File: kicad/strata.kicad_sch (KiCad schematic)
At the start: 100 parts, among them J1 Eurorack Mono Jack, J10 Conn_01x02_Male, J11 Conn_01x04_Male, J12 Conn_01x04_Female, J13 Conn_01x08_Male, J14 Eurorack Mono Jack, J15 Conn_01x08_Female, J16 Eurorack Mono Jack, J17 Eurorack Mono Jack, J18 Eurorack Mono Jack, J19 Eurorack Mono Jack, J2 Eurorack Mono Jack, J20 Eurorack Mono Jack, J24 Eurorack Mono Jack, J25 Eurorack Mono Jack, J26 Eurorack Mono Jack, J27 Eurorack Mono Jack, J28 Eurorack Mono Jack, J29 Eurorack Mono Jack, J3 Eurorack Mono Jack, J30 Eurorack Mono Jack, J31 Eurorack Mono Jack, J32 Conn_01x06_Female, J33 Eurorack Mono Jack, J34 Conn_01x06_Male, J35 Conn_01x08_Female, J36 Conn_01x08_Male, J37 Eurorack Power Small, J38 Conn_02x04_Odd_Even, J39 Conn_01x03_Male, J4 Eurorack Mono Jack, J49 Eurorack Mono Jack, J5 Conn_01x04_Female, J50 Eurorack Mono Jack, J51 Eurorack Mono Jack, J52 Conn_01x04_Female, J53 Conn_01x04_Male, J6 Conn_01x06_Female, J7 Conn_01x04_Male, J8 Conn_01x06_Male, J9 Conn_01x02_Female, Q17 2N3904, U1 TL072, U2 L78L05_TO92

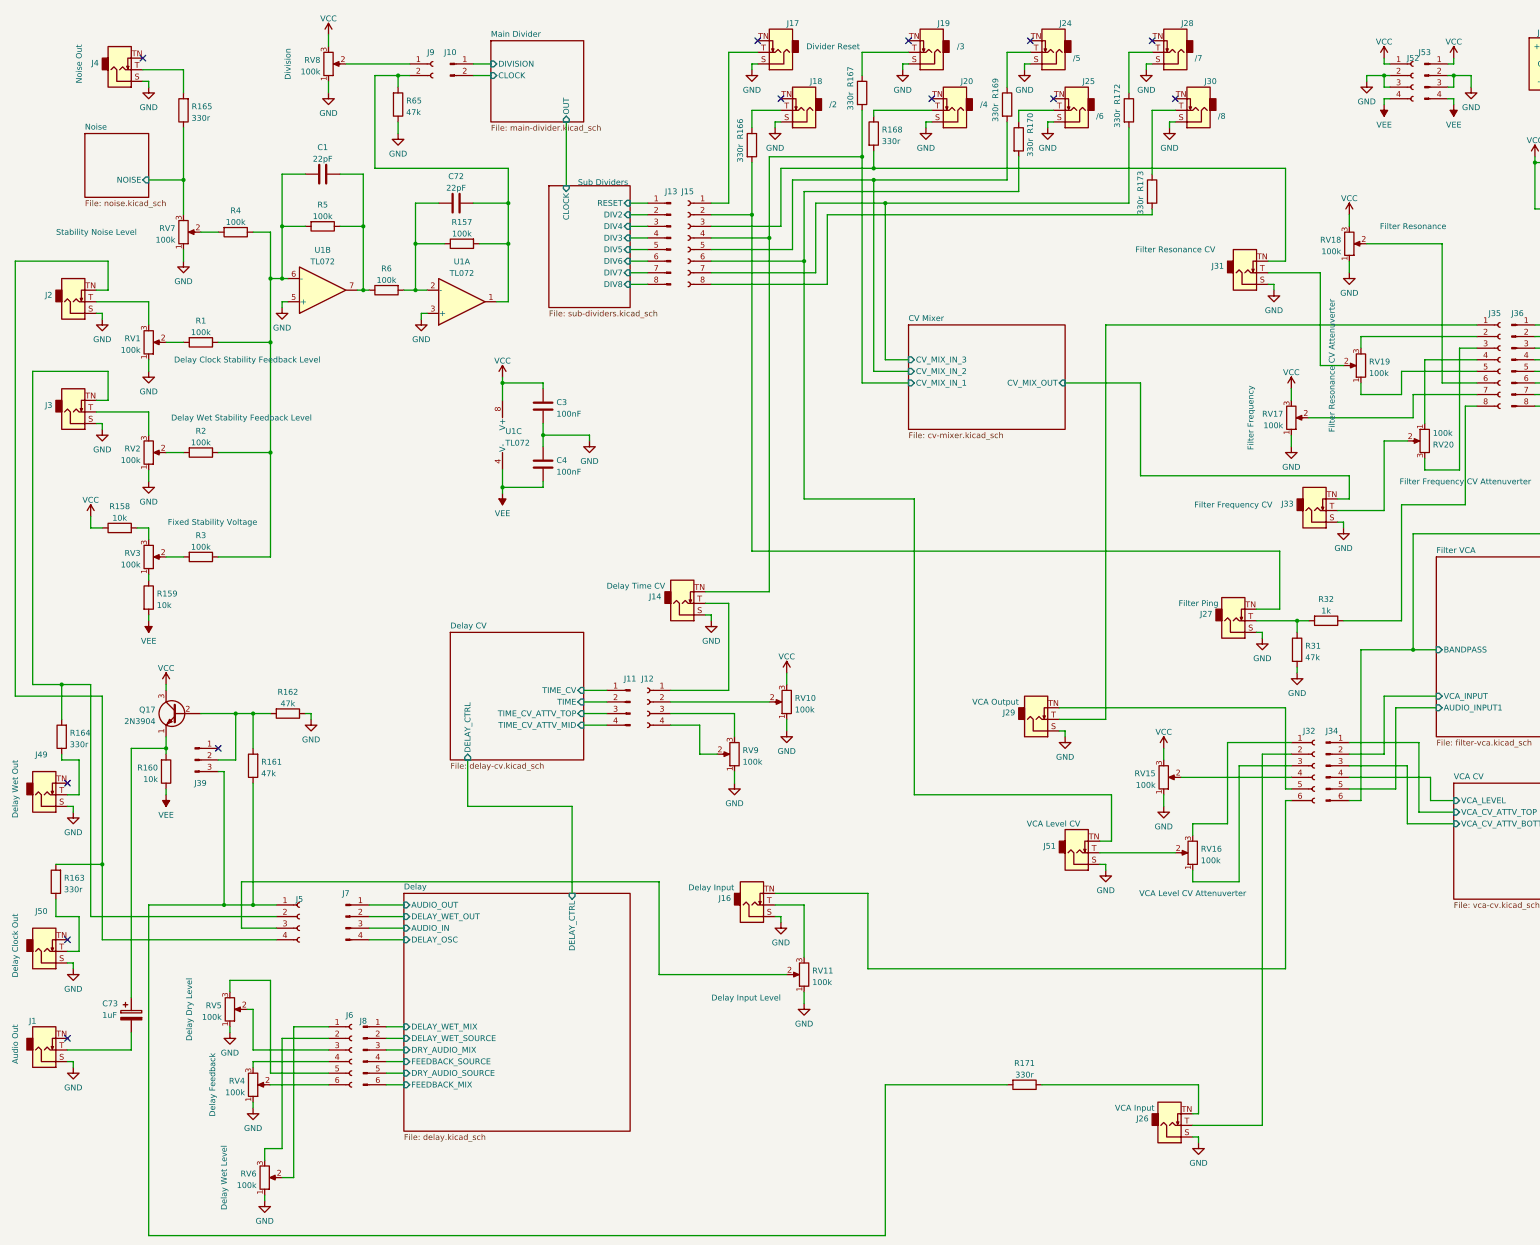
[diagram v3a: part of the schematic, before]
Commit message: Full rejig to use attiny for divider
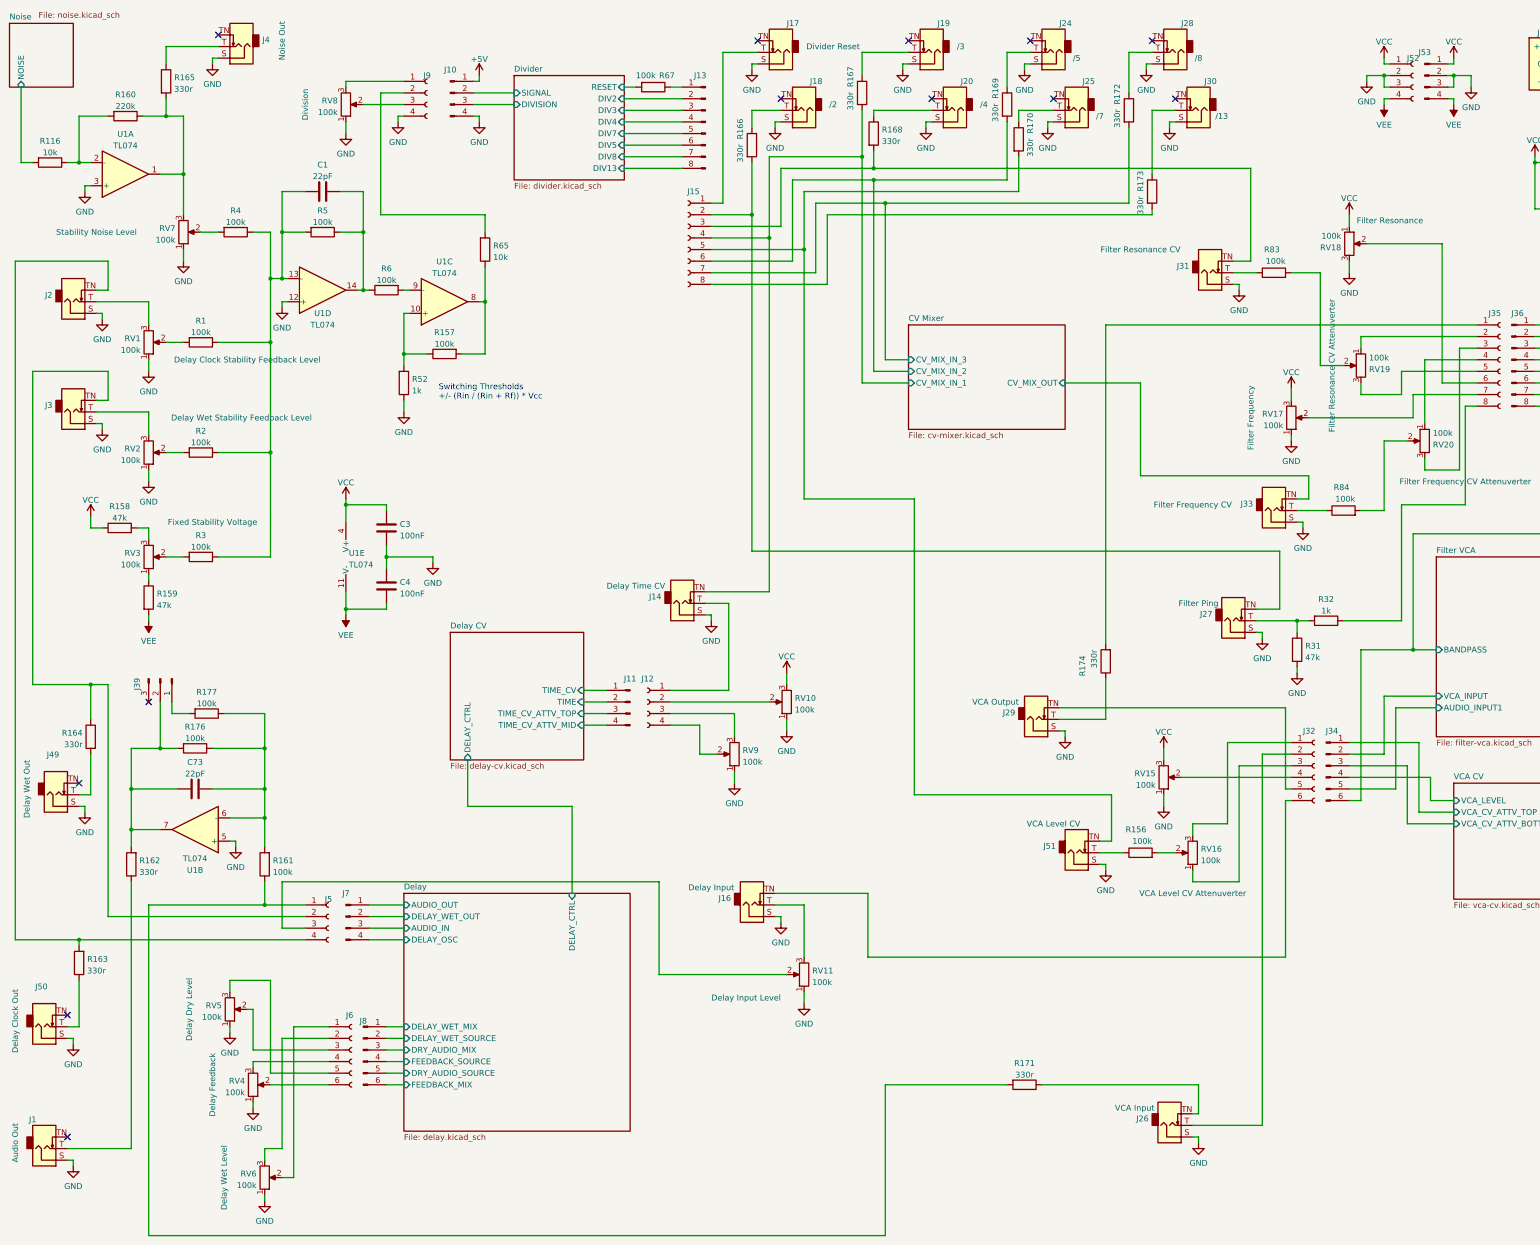
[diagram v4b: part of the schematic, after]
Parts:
- removed C72: 22pF, rumblesan-standard-parts:C_Rect_L7.0mm_W2.5mm_P5.00mm, symbol rumblesan-standard-parts:C
- removed C73: 1uF, rumblesan-standard-parts:CP_Radial_D5.0mm_P2.00mm, symbol rumblesan-standard-parts:C_Polarized
- removed J10: Conn_01x02_Male, Connector_PinHeader_2.54mm:PinHeader_1x02_P2.54mm_Vertical, symbol Connector:Conn_01x02_Male
- removed J9: Conn_01x02_Female, Connector_PinSocket_2.54mm:PinSocket_1x02_P2.54mm_Vertical, symbol Connector:Conn_01x02_Female
- removed Q17: 2N3904, Package_TO_SOT_THT:TO-92_Inline_Wide, symbol Transistor_BJT:2N3904
- removed U1: TL072, rumblesan-standard-parts:DIP-8_W7.62mm_Socket, symbol Amplifier_Operational:TL072
- added C73: 22pF, rumblesan-standard-parts:C_Rect_L7.0mm_W2.5mm_P5.00mm, symbol rumblesan-standard-parts:C
- added J10: Conn_01x04_Male, Connector_PinHeader_2.54mm:PinHeader_1x04_P2.54mm_Vertical, symbol Connector:Conn_01x04_Male
- added J9: Conn_01x04_Female, Connector_PinSocket_2.54mm:PinSocket_1x04_P2.54mm_Vertical, symbol Connector:Conn_01x04_Female
- added R116: 10k, rumblesan-standard-parts:R_Axial_DIN0207_L6.3mm_D2.5mm_P10.16mm_Horizontal, symbol rumblesan-standard-parts:R
- added R156, R176, R177, R67, R83, R84: 100k, rumblesan-standard-parts:R_Axial_DIN0207_L6.3mm_D2.5mm_P10.16mm_Horizontal, symbol rumblesan-standard-parts:R
- added R174: 330r, rumblesan-standard-parts:R_Axial_DIN0207_L6.3mm_D2.5mm_P10.16mm_Horizontal, symbol rumblesan-standard-parts:R
- added R52: 1k, rumblesan-standard-parts:R_Axial_DIN0207_L6.3mm_D2.5mm_P10.16mm_Horizontal, symbol rumblesan-standard-parts:R
- added U1: TL074, rumblesan-standard-parts:DIP-14_W7.62mm_Socket, symbol Amplifier_Operational:TL074
- C3, C4: Spec ceramic C0G -> ceramic X7R
- J25: Name /6 -> /7
- J28: Name /7 -> /8
- J30: Name /8 -> /13
- R158, R159: value 10k -> 47k
- R160: value 10k -> 220k
- R161: value 47k -> 100k
- R162: value 47k -> 330r; footprint rumblesan-standard-parts:R_Axial_DIN0207_L6.3mm_D2.5mm_P2.54mm_Vertical -> rumblesan-standard-parts:R_Axial_DIN0207_L6.3mm_D2.5mm_P10.16mm_Horizontal
- R164: footprint rumblesan-standard-parts:R_Axial_DIN0207_L6.3mm_D2.5mm_P2.54mm_Vertical -> rumblesan-standard-parts:R_Axial_DIN0207_L6.3mm_D2.5mm_P10.16mm_Horizontal
- R65: value 47k -> 10k
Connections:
- net +5V: now also J10.1 (Pin_1)
- net CV Mixer/CV_MIX_IN_2: now also J15.6 (Pin_6); no longer J15.5 (Pin_5)
- net GND: now also RV18.3, J10.4 (Pin_4), J9.4 (Pin_4), R52.1, U1.12 (+), U1.3 (+), U1.5 (+); no longer R162.1, R65.1, RV18.1
- net Noise/NOISE: now also R116.2; no longer R165.1, RV7.3
- net VCC: now also RV18.1, U1.4 (V+); no longer RV18.3, RV8.3
- net VEE: now also U1.11 (V-); no longer R160.1
- net at R157.2: now also R65.1, U1.8; no longer R65.2
- net at R157.1: now also R52.2, U1.10 (+); no longer R6.2
- net at R165.2: now also R160.1, RV7.3, U1.1; no longer J4.T (Tip)
- net at J5.1 (Pin_1), R161.1, R171.2: no longer J39.3 (Pin_3)
- net at C1.1, R1.1, R2.1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: now also U1.13 (-)
- net at J3.TN (Tip_normalize), J5.2 (Pin_2): now also R164.1; no longer R164.2
- net at J49.T (Tip): now also R164.2; no longer R164.1
- net at C1.2, R5.1, R6.1: now also U1.14
- net at J35.1 (Pin_1): now also R174.2; no longer J29.T (Tip)
- net at J35.2 (Pin_2): now also RV19.1; no longer RV19.3
- net at J35.5 (Pin_5): now also RV19.3; no longer RV19.1
- net at R160.2: now also R116.1, U1.2 (-)
- net at J39.2 (Pin_2), R162.2: now also C73.2, R176.2, U1.7; no longer R161.2
- net at J31.T (Tip): now also R83.1; no longer RV19.2
- net at J33.T (Tip): now also R84.1; no longer RV20.2
- net at J51.TN (Tip_normalize), R170.2: now also J15.5 (Pin_5); no longer J15.6 (Pin_6)
- net at J51.T (Tip): now also R156.1; no longer RV16.2
- net at RV8.2: now also J9.3 (Pin_3)
- net at J1.T (Tip): now also R162.1
- net at J39.1 (Pin_1): now also R177.2
- net Sub Dividers/DIV2 renamed Divider/DIV2
- net Sub Dividers/DIV3 renamed Divider/DIV4
- net Sub Dividers/DIV4 renamed Divider/DIV3
- net Sub Dividers/DIV5 renamed Divider/DIV7
- net Sub Dividers/DIV6 renamed Divider/DIV5
- net Sub Dividers/DIV7 renamed Divider/DIV8
- net Sub Dividers/DIV8 renamed Divider/DIV13
- net Sub Dividers/RESET: no longer names the net of J13.1 (Pin_1)
- net Sub Dividers/RESET: now also R67.1
- new net: J4.T (Tip), R165.1
- new net: R84.2, RV20.2
- new net: J9.2 (Pin_2), R65.2
- new net: C73.1, R161.2, R176.1, R177.1, U1.6 (-)
- new net: R156.2, RV16.2
- new net: R83.2, RV19.2
- new net: R6.2, U1.9 (-)
- new net: J9.1 (Pin_1), RV8.3
- new net: J29.T (Tip), R174.1
- new net Divider/DIVISION: J10.3 (Pin_3)
- new net Divider/RESET: R67.2
- new net Divider/SIGNAL: J10.2 (Pin_2)
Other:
- removed sheet Main Divider
- removed sheet Sub Dividers
- added sheet Divider (divider.kicad_sch)
- note added: "Switching Thresholds +/- (Rin / (Rin + Rf)) * Vcc"
- moved on the sheet: C1, C3, C4, J1, J13, J31, J33, J4, J49, J5, J50, R157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

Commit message: Finished most recent redesign
probably still needs fixing though
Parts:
- C6: footprint rumblesan-standard-parts:CP_Radial_D5.0mm_P2.00mm -> rumblesan-standard-parts:CP_Radial_D5.0mm_L11.0mm_P2.00mm_Horizontal
- C7: footprint rumblesan-standard-parts:CP_Radial_D5.0mm_P2.00mm -> rumblesan-standard-parts:CP_Radial_D6.3.0mm_L11.0mm_P2.00mm_Horizontal
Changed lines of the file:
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@@
       (effects (font (size 1.27 1.27)) (justify left))
     )
-    (property "Footprint" "rumblesan-standard-parts:CP_Radial_D5.0mm_P2.00mm" (id 2) (at 401.32 51.1048 0)
+    (property "Footprint" "rumblesan-standard-parts:CP_Radial_D6.3.0mm_L11.0mm_P2.00mm_Horizontal" (id 2) (at 401.32 51.1048 0)
       (effects (font (size 1.27 1.27)) hide)
     )
@@
       (effects (font (size 1.27 1.27)) (justify left))
     )
-    (property "Footprint" "rumblesan-standard-parts:CP_Radial_D5.0mm_P2.00mm" (id 2) (at 401.32 38.4048 0)
+    (property "Footprint" "rumblesan-standard-parts:CP_Radial_D5.0mm_L11.0mm_P2.00mm_Horizontal" (id 2) (at 401.32 38.4048 0)
       (effects (font (size 1.27 1.27)) hide)
     )
@@
     )
     (path "/d1c4b4fd-5762-4000-9df8-83bd7b665ce2"
-      (reference "C6") (unit 1) (value "10uF") (footprint "rumblesan-standard-parts:CP_Radial_D5.0mm_P2.00mm")
+      (reference "C6") (unit 1) (value "10uF") (footprint "rumblesan-standard-parts:CP_Radial_D5.0mm_L11.0mm_P2.00mm_Horizontal")
     )
     (path "/5bf0b729-aac6-4585-bac0-2e1a7ffbf3b9"
-      (reference "C7") (unit 1) (value "10uF") (footprint "rumblesan-standard-parts:CP_Radial_D5.0mm_P2.00mm")
+      (reference "C7") (unit 1) (value "10uF") (footprint "rumblesan-standard-parts:CP_Radial_D6.3.0mm_L11.0mm_P2.00mm_Horizontal")
     )
     (path "/256127d0-0479-4408-a803-d00b3565e635/8fedaf81-144e-4069-b4a7-05f99da9d028"
@@
     )
     (path "/256127d0-0479-4408-a803-d00b3565e635/1b5de37d-f3ae-40d3-a60b-d8d12b5426c7"
-      (reference "C13") (unit 1) (value "10uF") (footprint "rumblesan-standard-parts:CP_Radial_D5.0mm_P2.00mm")
+      (reference "C13") (unit 1) (value "10uF") (footprint "rumblesan-standard-parts:CP_Radial_D5.0mm_L11.0mm_P2.00mm_Horizontal")
     )
     (path "/256127d0-0479-4408-a803-d00b3565e635/0ee6ea30-0dc3-4184-ab6a-486efb66e095"
@@
     )
     (path "/256127d0-0479-4408-a803-d00b3565e635/4ddf042e-9ddf-4a8b-ab4d-2df4486c7e7c"
-      (reference "C15") (unit 1) (value "47uF") (footprint "rumblesan-standard-parts:CP_Radial_D6.3mm_P2.50mm")
+      (reference "C15") (unit 1) (value "47uF") (footprint "rumblesan-standard-parts:CP_Radial_D6.3.0mm_L11.0mm_P2.00mm_Horizontal")
     )
     (path "/256127d0-0479-4408-a803-d00b3565e635/082bd943-8af9-4b2e-8f31-bb791b0964d9"
@@
     )
     (path "/256127d0-0479-4408-a803-d00b3565e635/102388f9-bcb5-4437-9670-f018267c112d"
-      (reference "C22") (unit 1) (value "10uF") (footprint "rumblesan-standard-parts:CP_Radial_D5.0mm_P2.00mm")
+      (reference "C22") (unit 1) (value "10uF") (footprint "rumblesan-standard-parts:CP_Radial_D5.0mm_L11.0mm_P2.00mm_Horizontal")
     )
     (path "/256127d0-0479-4408-a803-d00b3565e635/e173a745-e0e9-41c9-8c9e-35e00d5410da"
@@
     )
     (path "/256127d0-0479-4408-a803-d00b3565e635/cfa276a3-83d0-46c5-a5a0-39e4701f402c"
-      (reference "C28") (unit 1) (value "10uF") (footprint "rumblesan-standard-parts:CP_Radial_D5.0mm_P2.00mm")
+      (reference "C28") (unit 1) (value "10uF") (footprint "rumblesan-standard-parts:CP_Radial_D5.0mm_L11.0mm_P2.00mm_Horizontal")
     )
     (path "/256127d0-0479-4408-a803-d00b3565e635/5b3cb3f1-de45-4f03-9b3f-67f18e354dc1"
@@
       (reference "R67") (unit 1) (value "100k") (footprint "rumblesan-standard-parts:R_Axial_DIN0207_L6.3mm_D2.5mm_P10.16mm_Horizontal")
     )
-    (path "/e95780cf-5325-4c64-89b1-e833ad4ca347/cf287e32-83db-4d95-b555-cb6fd8f0b072"
-      (reference "R69") (unit 1) (value "1k8") (footprint "rumblesan-standard-parts:R_Axial_DIN0207_L6.3mm_D2.5mm_P10.16mm_Horizontal")
-    )
     (path "/e95780cf-5325-4c64-89b1-e833ad4ca347/215e002a-fe0a-440d-bc38-e5f4fd99c70e"
       (reference "R70") (unit 1) (value "1k") (footprint "rumblesan-standard-parts:R_Axial_DIN0207_L6.3mm_D2.5mm_P10.16mm_Horizontal")
     )
-    (path "/e95780cf-5325-4c64-89b1-e833ad4ca347/0762d879-9936-4bf1-a6e6-93cb741522de"
-      (reference "R71") (unit 1) (value "1k8") (footprint "rumblesan-standard-parts:R_Axial_DIN0207_L6.3mm_D2.5mm_P10.16mm_Horizontal")
-    )
     (path "/e95780cf-5325-4c64-89b1-e833ad4ca347/64f7b38d-bf0c-423d-bae7-001544df3970"
       (reference "R72") (unit 1) (value "1k") (footprint "rumblesan-standard-parts:R_Axial_DIN0207_L6.3mm_D2.5mm_P10.16mm_Horizontal")
     )
-    (path "/e95780cf-5325-4c64-89b1-e833ad4ca347/8bc4bf34-8080-4ff2-a810-c54c4b2c947b"
-      (reference "R73") (unit 1) (value "1k8") (footprint "rumblesan-standard-parts:R_Axial_DIN0207_L6.3mm_D2.5mm_P10.16mm_Horizontal")
-    )
     (path "/e95780cf-5325-4c64-89b1-e833ad4ca347/3a288079-30d1-4053-b377-aeb9a0d3b1a6"
       (reference "R74") (unit 1) (value "1k") (footprint "rumblesan-standard-parts:R_Axial_DIN0207_L6.3mm_D2.5mm_P10.16mm_Horizontal")
     )
-    (path "/e95780cf-5325-4c64-89b1-e833ad4ca347/9ebb3c9a-c489-4fd2-9076-81960b172046"
-      (reference "R75") (unit 1) (value "1k8") (footprint "rumblesan-standard-parts:R_Axial_DIN0207_L6.3mm_D2.5mm_P10.16mm_Horizontal")
-    )
     (path "/e95780cf-5325-4c64-89b1-e833ad4ca347/2506db83-0c04-4901-b2bc-2bd68f6a4e26"
       (reference "R76") (unit 1) (value "1k") (footprint "rumblesan-standard-parts:R_Axial_DIN0207_L6.3mm_D2.5mm_P10.16mm_Horizontal")
     )
-    (path "/e95780cf-5325-4c64-89b1-e833ad4ca347/1d6f62e1-b37d-4f54-9c75-1308479d7d4e"
-      (reference "R77") (unit 1) (value "1k8") (footprint "rumblesan-standard-parts:R_Axial_DIN0207_L6.3mm_D2.5mm_P10.16mm_Horizontal")
-    )
     (path "/e95780cf-5325-4c64-89b1-e833ad4ca347/a3f17647-9565-45a7-af46-4e2bad736f21"
       (reference "R78") (unit 1) (value "1k") (footprint "rumblesan-standard-parts:R_Axial_DIN0207_L6.3mm_D2.5mm_P10.16mm_Horizontal")
     )
-    (path "/e95780cf-5325-4c64-89b1-e833ad4ca347/02258eb4-e7a4-487d-a963-9d643445b804"
-      (reference "R79") (unit 1) (value "1k8") (footprint "rumblesan-standard-parts:R_Axial_DIN0207_L6.3mm_D2.5mm_P10.16mm_Horizontal")
-    )
     (path "/e95780cf-5325-4c64-89b1-e833ad4ca347/9fed4e9e-d926-4b2f-9ba9-4003142b92dc"
       (reference "R80") (unit 1) (value "1k") (footprint "rumblesan-standard-parts:R_Axial_DIN0207_L6.3mm_D2.5mm_P10.16mm_Horizontal")
     )
-    (path "/e95780cf-5325-4c64-89b1-e833ad4ca347/507ad553-eb3d-4d6f-9d6d-754d254a6982"
-      (reference "R81") (unit 1) (value "1k8") (footprint "rumblesan-standard-parts:R_Axial_DIN0207_L6.3mm_D2.5mm_P10.16mm_Horizontal")
-    )
     (path "/e95780cf-5325-4c64-89b1-e833ad4ca347/528ee385-65d5-4ab2-9c25-324bf7b689bd"
